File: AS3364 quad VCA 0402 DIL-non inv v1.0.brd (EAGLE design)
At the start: 41.3 x 16.2 mm, 45 parts, among them IC1 TL072JD, IC2 TL072JD

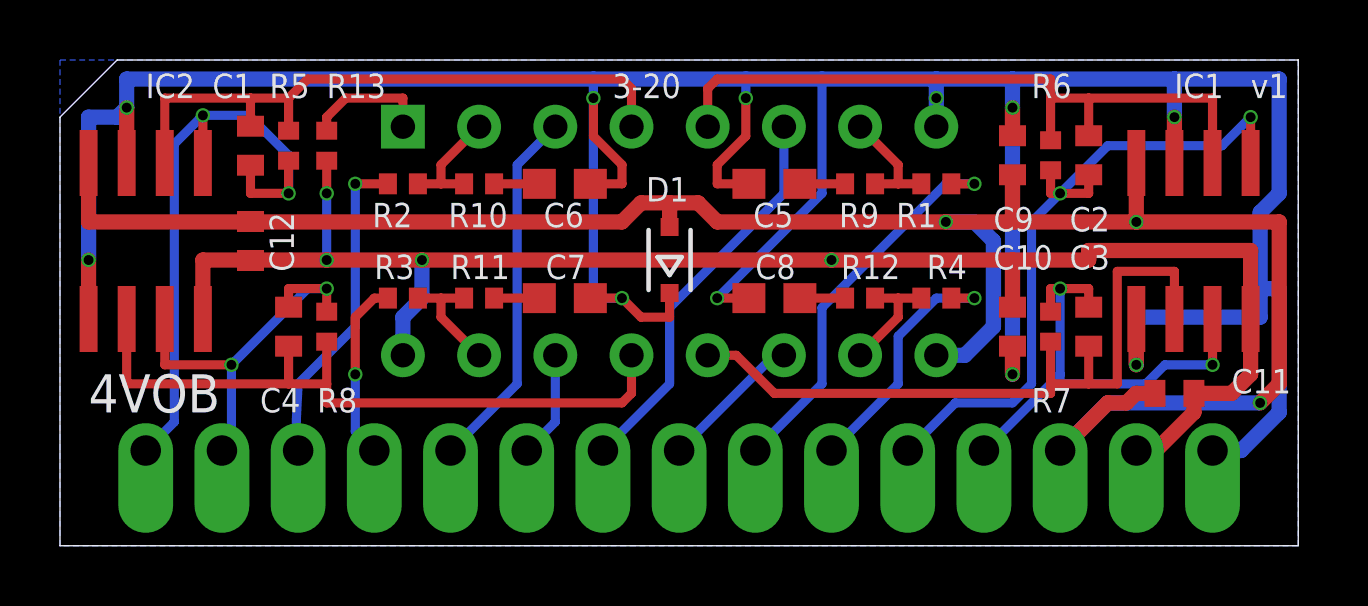
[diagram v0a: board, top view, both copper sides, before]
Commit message: Added AS3364 versions of quad VCA
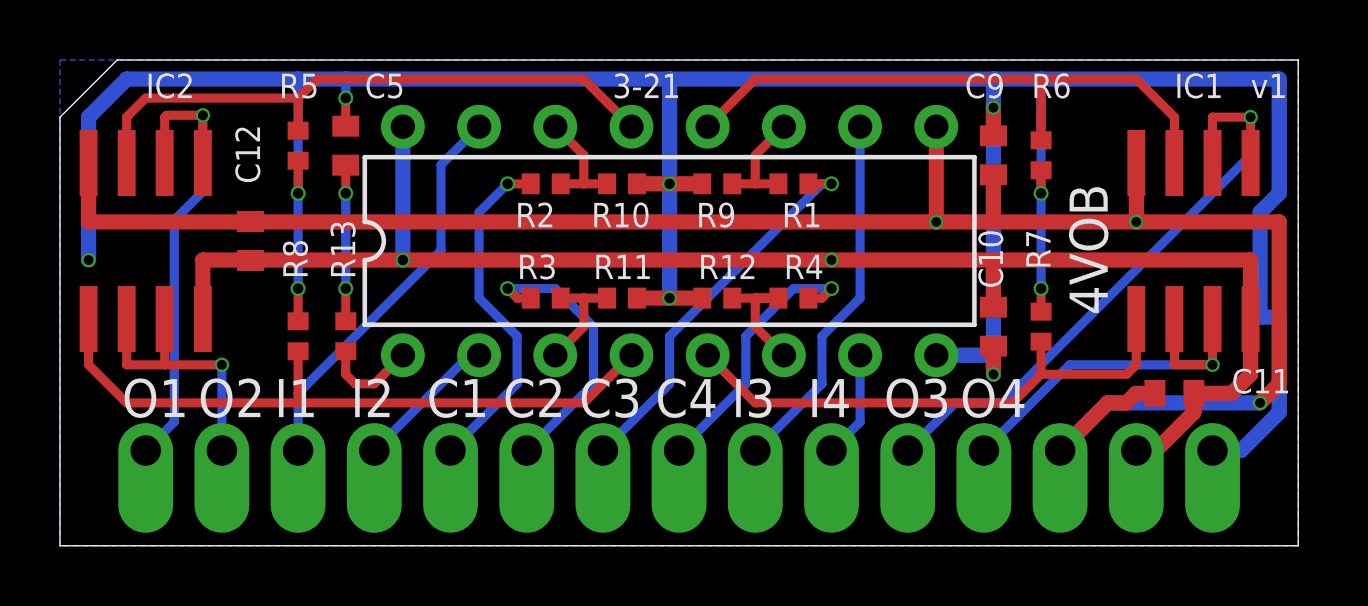
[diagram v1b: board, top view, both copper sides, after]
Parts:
- removed C1, C2, C3, C4: 100pF, rcl:C0402
- removed C6, C7, C8: 560pF, rcl:C0603
- removed D1: B5817, diode:SOD323-R
- removed DA1: V2164D, ic-coolaudio:DIP-16
- added DA2: AS3364D, joakim:DIL16J
- C5: value 560pF -> 5nF; device rcl:C0603 -> rcl:C0402
- R1, R2, R3, R4, R5, R6, R7, R8: value 30k -> 47k
- R10, R11, R12, R9: value 500R -> 47k
- R13: value 7.5k for A -> 100R
- moved C5 14.3 mm to (9.53, 13.3), turned to 270 degrees
- moved R13 6.38 mm to (9.53, 6.99), turned to 270 degrees
- moved R12 4.76 mm to (21.9, 8.26)
- moved R9 4.76 mm to (21.9, 12.1)
- moved R10 4.76 mm to (18.7, 12.1)
- moved R11 4.76 mm to (18.7, 8.26)
- moved R1 4.76 mm to (24.4, 12.1)
- moved R2 4.76 mm to (16.2, 12.1)
- moved R3 4.76 mm to (16.2, 8.26)
- moved R4 4.76 mm to (24.4, 8.26)
- moved R8 1.00 mm to (7.94, 6.99), turned to 270 degrees
- moved C10 0.64 mm to (31.1, 7.30)
- moved C9 0.64 mm to (31.1, 13.0)
- moved R6 0.32 mm to (32.7, 13.0), turned to 90 degrees
- moved R7 0.32 mm to (32.7, 7.30), turned to 270 degrees
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- renumbered +15V to +12V, -15V to -12V
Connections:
- removed net +15V: +12V.1, C10.2, C11.2, C12.2, DA1.16, IC1.8, IC2.8, R13.1
- removed net -15V: -12V.1, C11.1, C12.1, C9.1, D1.A, DA1.9, IC1.4, IC2.4
- removed net C1: CV1.1, DA1.3
- removed net C2: CV2.1, DA1.14
- removed net C3: CV3.1, DA1.6
- removed net C4: CV4.1, DA1.11
- removed net N$1: C4.1, DA1.13, IC2.6, R8.1
- removed net N$17: DA1.7, R1.2, R9.2
- removed net N$18: DA1.2, R10.2, R2.2
- removed net N$19: DA1.15, R11.2, R3.2
- removed net N$20: DA1.10, R12.2, R4.2
- removed net N$3: C3.1, DA1.12, IC1.6, R7.1
- removed net N$5: C2.1, DA1.5, IC1.2, R6.1
- removed net N$7: C1.1, DA1.4, IC2.2, R5.1
- removed net N$9: C5.2, R9.1
- new net +12V: +12V.1, C10.2, C11.2, C12.2, DA2.16, IC1.8, IC2.8
- new net -12V: -12V.1, C11.1, C12.1, C9.1, DA2.9, IC1.4, IC2.4
- new net CV1: CV1.1, R2.1
- new net CV2: CV2.1, R3.1
- new net CV2_IN: DA2.3, R11.2, R3.2
- new net CV3: CV3.1, R1.1
- new net CV4: CV4.1, R4.1
- new net N$13: DA2.13, IC2.3, R5.2
- new net N$14: C5.2, R13.1
- new net N$21: DA2.14, R10.2, R2.2
- new net N$4: DA2.4, IC2.5, R8.2
- new net N$6: DA2.5, IC1.5, R7.2
- net GND: now also DA2.8, R10.1, R11.1, R12.1, R5.1, R6.1, R7.1, R8.1, R9.1; no longer C6.1, C7.1, C8.1, D1.C, DA1.8, IC1.3, IC1.5, IC2.3, IC2.5
- net IN1: now also DA2.15; no longer R2.1
- net IN2: now also DA2.2; no longer R3.1
- net IN3: now also DA2.10; no longer R1.1
- net IN4: now also DA2.7; no longer R4.1
- net N$10: now also DA2.6, R12.2, R4.2; no longer C6.2, R10.1
- net N$11: now also DA2.12, IC1.3, R6.2; no longer C7.2, R11.1
- net N$12: now also DA2.11, R1.2, R9.2; no longer C8.2, R12.1
- net N$2: now also DA2.1; no longer DA1.1
- net OUT1: now also IC2.2; no longer C1.2, R5.2
- net OUT2: now also IC2.6; no longer C4.2, R8.2
- net OUT3: now also IC1.2; no longer C2.2, R6.2
- net OUT4: now also IC1.6; no longer C3.2, R7.2
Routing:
- net -15V: track 71.1 -> 0.00 mm, vias 3 -> 0
- net -12V: track 0.00 -> 65.9 mm, vias 0 -> 3
- net +15V: track 54.9 -> 0.00 mm, vias 4 -> 0
- net +12V: track 0.00 -> 52.0 mm, vias 0 -> 2
- net N$3: track 24.4 -> 0.00 mm
- net N$1: track 23.7 -> 0.00 mm
- net N$5: track 23.7 -> 0.00 mm
- net N$4: track 0.00 -> 22.5 mm
- net N$7: track 21.4 -> 0.00 mm
- net N$13: track 0.00 -> 20.6 mm
- net N$11: track 1.51 -> 20.3 mm
- net N$6: track 0.00 -> 18.1 mm
- net GND: track 119.4 -> 104.3 mm, vias 11 -> 10
- net C3: track 13.3 -> 0.00 mm
- net CV3: track 0.00 -> 13.0 mm, vias 0 -> 1
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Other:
- board text added: "+12v"
- board text added: "-12v"
- board text added: "3-21"
- board text added: "NB: Max 26V diff"
- board text added: "Quad linear VCA"
- board text removed: "+15v"
- board text removed: "-15v"
- board text removed: "3-20"
- board text removed: "Mount socket on this side!"
- board text removed: "Quad exp VCA"

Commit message: Turned pads to make it possible to solder angled legs
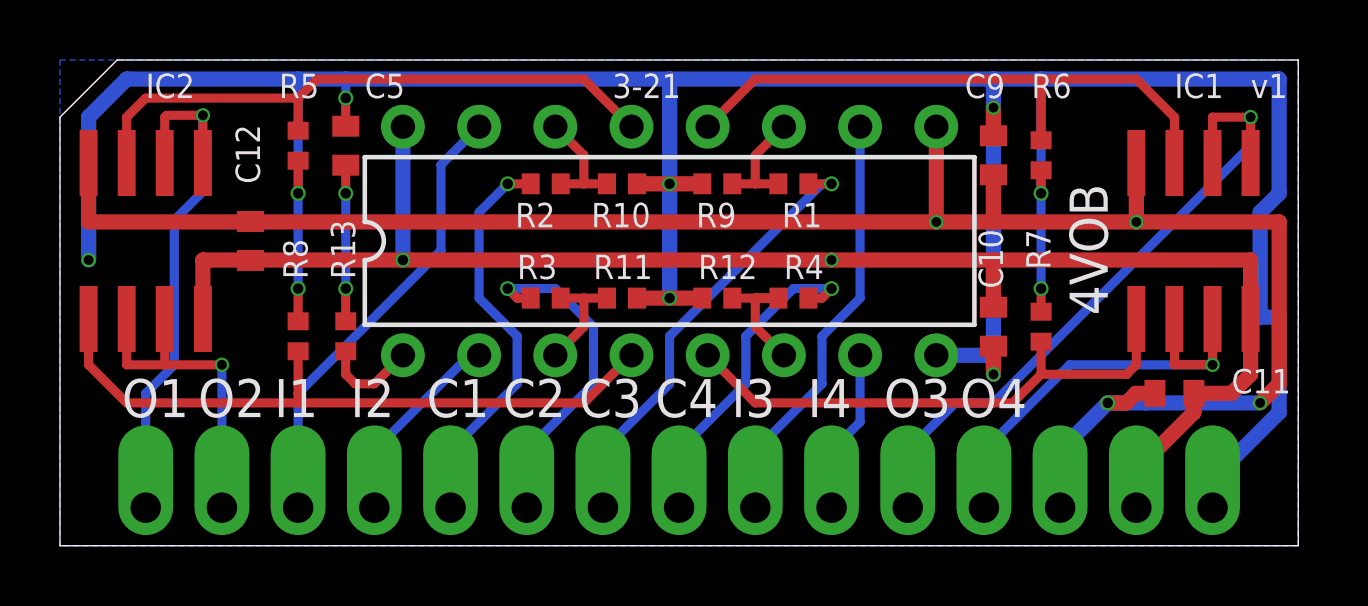
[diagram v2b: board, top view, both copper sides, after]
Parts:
- moved +12V 1.90 mm to (35.9, 1.27), turned to 180 degrees
- moved -12V 1.90 mm to (33.3, 1.27), turned to 180 degrees
- moved CV1 1.90 mm to (13.0, 1.27), turned to 180 degrees
- moved CV2 1.90 mm to (15.6, 1.27), turned to 180 degrees
- moved CV3 1.90 mm to (18.1, 1.27), turned to 180 degrees
- moved CV4 1.90 mm to (20.6, 1.27), turned to 180 degrees
- moved GND 1.90 mm to (38.4, 1.27), turned to 180 degrees
- moved IN1 1.90 mm to (7.94, 1.27), turned to 180 degrees
- moved IN2 1.90 mm to (10.5, 1.27), turned to 180 degrees
- moved IN3 1.90 mm to (23.2, 1.27), turned to 180 degrees
- moved IN4 1.90 mm to (25.7, 1.27), turned to 180 degrees
- moved OUT1 1.90 mm to (2.86, 1.27), turned to 180 degrees
- moved OUT2 1.90 mm to (5.40, 1.27), turned to 180 degrees
- moved OUT3 1.90 mm to (28.3, 1.27), turned to 180 degrees
- moved OUT4 1.90 mm to (30.8, 1.27), turned to 180 degrees
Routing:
- net IN1: track 13.3 -> 15.2 mm
- net CV4: track 9.15 -> 11.1 mm
- net CV3: track 13.0 -> 14.9 mm
- net IN2: track 4.81 -> 6.71 mm
- net IN4: track 3.57 -> 5.47 mm
- net OUT4: track 13.1 -> 15.0 mm
- net OUT2: track 9.09 -> 11.0 mm
- net CV2: track 9.33 -> 11.2 mm
- net CV1: track 11.5 -> 13.4 mm
- net OUT1: track 16.4 -> 18.3 mm
- net IN3: track 12.2 -> 14.1 mm
- net OUT3: track 21.1 -> 22.8 mm
- net +12V: track 52.0 -> 53.5 mm
- net GND: track 104.3 -> 105.6 mm
- net -12V: track 65.9 -> 65.6 mm, vias 3 -> 4

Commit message: Checked most things, changed CV input resistors, added cap to mixer output
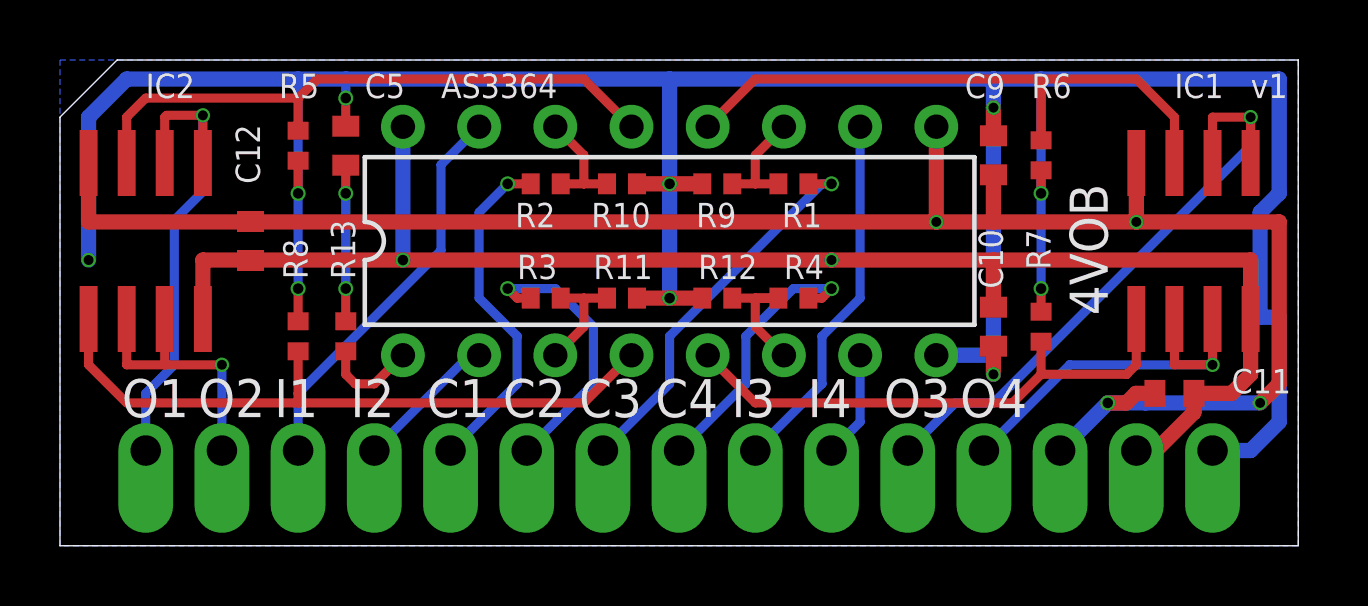
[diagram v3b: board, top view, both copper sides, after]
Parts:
- R1, R2, R3, R4: value 47k -> 33k
- R10, R11, R12, R9: value 47k -> 22k
- moved +12V 1.90 mm to (35.9, 3.17), turned to 0 degrees
- moved -12V 1.90 mm to (33.3, 3.17), turned to 0 degrees
- moved CV1 1.90 mm to (13.0, 3.17), turned to 0 degrees
- moved CV2 1.90 mm to (15.6, 3.17), turned to 0 degrees
- moved CV3 1.90 mm to (18.1, 3.17), turned to 0 degrees
- moved CV4 1.90 mm to (20.6, 3.17), turned to 0 degrees
- moved GND 1.90 mm to (38.4, 3.17), turned to 0 degrees
- moved IN1 1.90 mm to (7.94, 3.17), turned to 0 degrees
- moved IN2 1.90 mm to (10.5, 3.17), turned to 0 degrees
- moved IN3 1.90 mm to (23.2, 3.17), turned to 0 degrees
- moved IN4 1.90 mm to (25.7, 3.17), turned to 0 degrees
- moved OUT1 1.90 mm to (2.86, 3.17), turned to 0 degrees
- moved OUT2 1.90 mm to (5.40, 3.17), turned to 0 degrees
- moved OUT3 1.90 mm to (28.3, 3.17), turned to 0 degrees
- moved OUT4 1.90 mm to (30.8, 3.17), turned to 0 degrees
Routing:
- net OUT3: track 22.8 -> 20.9 mm
- net IN1: track 15.2 -> 13.3 mm
- net CV4: track 11.1 -> 9.15 mm
- net CV3: track 14.9 -> 13.0 mm
- net CV1: track 13.4 -> 11.5 mm
- net IN2: track 6.71 -> 4.81 mm
- net IN4: track 5.47 -> 3.57 mm
- net OUT4: track 15.0 -> 13.1 mm
- net OUT2: track 11.0 -> 9.09 mm
- net CV2: track 11.2 -> 9.33 mm
- net OUT1: track 18.3 -> 16.4 mm
- net IN3: track 14.1 -> 12.2 mm
- net -12V: track 65.6 -> 63.7 mm
- net +12V: track 53.5 -> 52.0 mm
- net GND: track 105.6 -> 104.5 mm
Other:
- board text added: "AS3364"
- board text removed: "3-21"

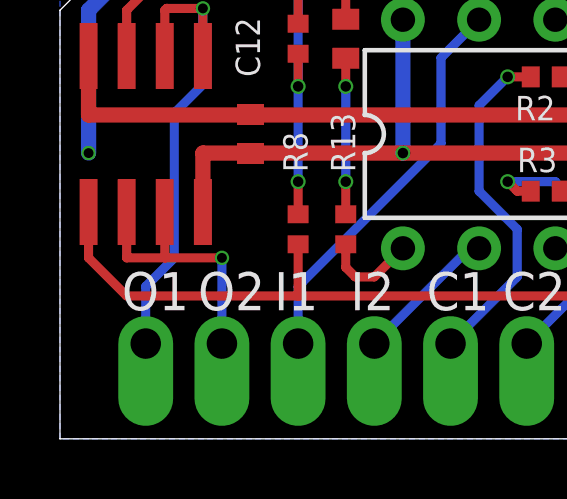
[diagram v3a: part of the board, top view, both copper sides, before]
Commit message: Almost finished bom/cpl
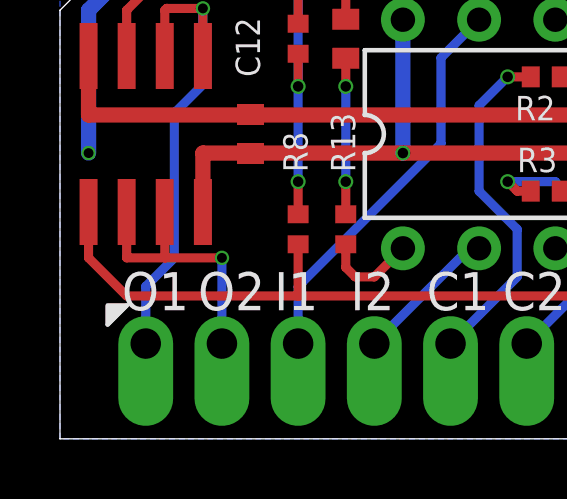
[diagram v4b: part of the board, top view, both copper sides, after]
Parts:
- removed +12V, -12V, CV1, CV2, CV3, CV4, GND, IN1, IN2, IN3, IN4, OUT1, OUT2, OUT3, OUT4: (no value), joakim:SIP-PIN01-1J
- added SV1: (no value), joakim:SIP-PIN15-1J
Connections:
- net +12V: now also SV1.14; no longer +12V.1
- net -12V: now also SV1.13; no longer -12V.1
- net CV1: now also SV1.5; no longer CV1.1
- net CV2: now also SV1.6; no longer CV2.1
- net CV3: now also SV1.7; no longer CV3.1
- net CV4: now also SV1.8; no longer CV4.1
- net GND: now also SV1.15; no longer GND.1
- net IN1: now also SV1.3; no longer IN1.1
- net IN2: now also SV1.4; no longer IN2.1
- net IN3: now also SV1.9; no longer IN3.1
- net IN4: now also SV1.10; no longer IN4.1
- net OUT1: now also SV1.1; no longer OUT1.1
- net OUT2: now also SV1.2; no longer OUT2.1
- net OUT3: now also SV1.11; no longer OUT3.1
- net OUT4: now also SV1.12; no longer OUT4.1
